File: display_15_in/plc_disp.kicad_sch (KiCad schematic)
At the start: 12 parts, among them M17 N-MOSFET, M18 N-MOSFET, M19 N-MOSFET, M20 N-MOSFET, U10 SA39-12YWA, U11 HDSP-7801, U13 SA39-12YWA, U14 HDSP-7801

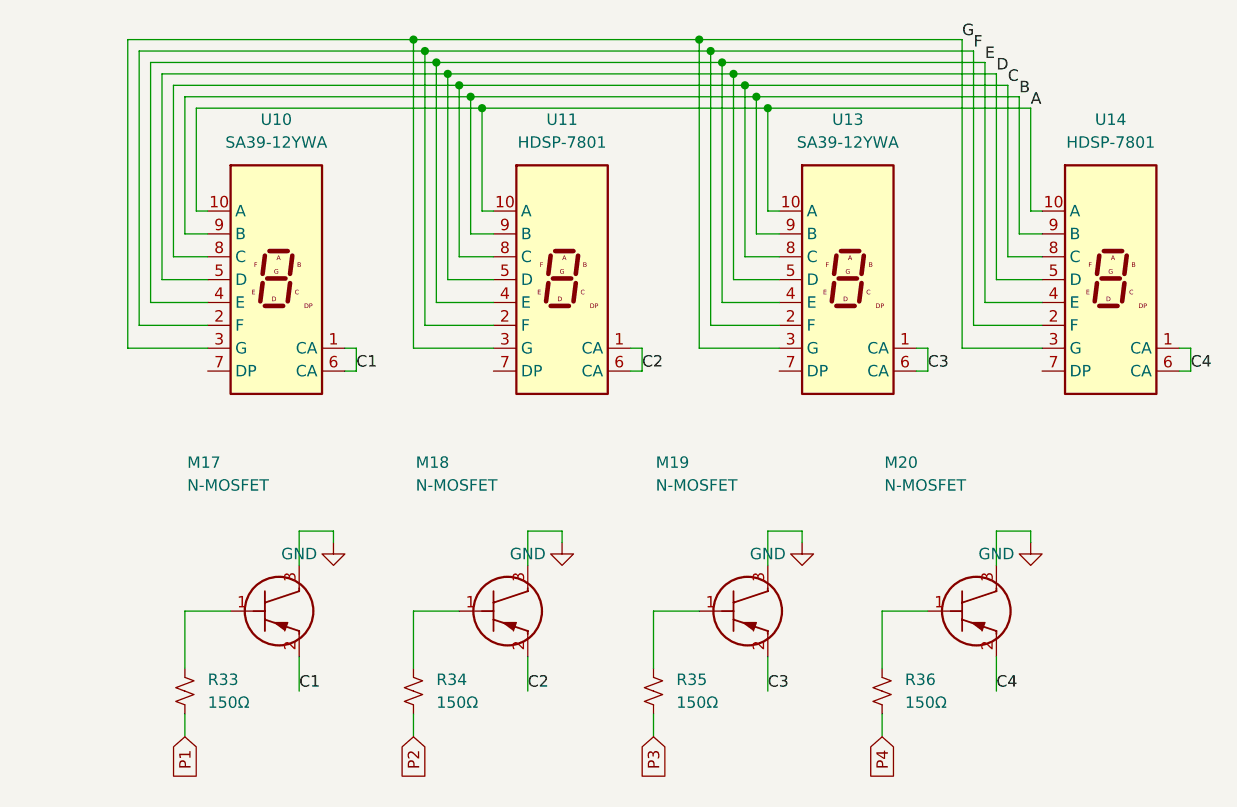
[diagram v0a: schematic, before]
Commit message: added full end of track display board
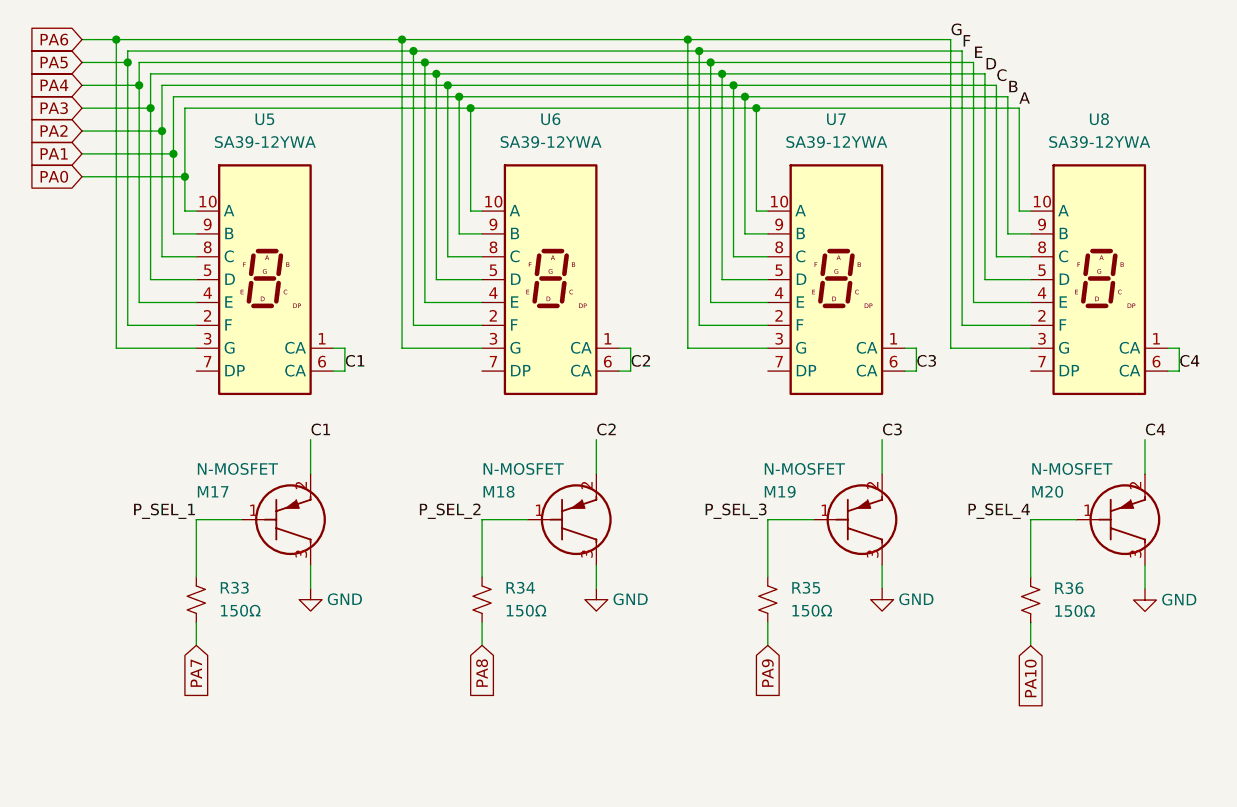
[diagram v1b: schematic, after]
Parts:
- removed U11, U14: HDSP-7801, Display_7Segment:HDSP-7801, symbol Display_Character:HDSP-7801
- removed U13: SA39-12YWA, Display_7Segment:Sx39-1xxxxx, symbol Display_Character:SA39-12YWA
- added U6, U7, U8: SA39-12YWA, 7-seg-1-inch:LDS-AA14RI, symbol Display_Character:SA39-12YWA
- R33, R34, R35, R36: footprint (none) -> Resistor_SMD:R_0805_2012Metric
- U5: renamed from U10; footprint Display_7Segment:Sx39-1xxxxx -> 7-seg-1-inch:LDS-AA14RI
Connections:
- net C2: now also U6.1 (CA), U6.6 (CA)
- net C3: now also U7.1 (CA), U7.6 (CA)
- net C4: now also U8.1 (CA), U8.6 (CA)
- net P_SEL_3: now reaches M19.1, R35.1
- net P_SEL_4: now reaches M20.1, R36.1
- net P_SEL_2: now reaches M18.1, R34.1
- net P_SEL_1: now reaches M17.1, R33.1
- net A renamed PA0
- net PA0: now also U6.10 (A), U7.10 (A), U8.10 (A)
- net B renamed PA1
- net PA1: now also U6.9 (B), U7.9 (B), U8.9 (B)
- net C renamed PA2
- net PA2: now also U6.8 (C), U7.8 (C), U8.8 (C)
- net D renamed PA3
- net PA3: now also U6.5 (D), U7.5 (D), U8.5 (D)
- net E renamed PA4
- net PA4: now also U6.4 (E), U7.4 (E), U8.4 (E)
- net F renamed PA5
- net PA5: now also U6.2 (F), U7.2 (F), U8.2 (F)
- net G renamed PA6
- net PA6: now also U6.3 (G), U7.3 (G), U8.3 (G)
- net P1 renamed PA7
- net P2 renamed PA8
- net P3 renamed PA9
- net P4 renamed PA10
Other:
- title: (none) -> Placement Display
- moved on the sheet: M17, M18, M19, M20, R33, R34, R35, R36, U5
